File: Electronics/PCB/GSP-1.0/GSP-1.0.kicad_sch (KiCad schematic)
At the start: 14 parts

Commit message: Fix ESP32 version
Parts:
- removed U3: (no value), symbol RF_Module:ESP32-WROOM-32
- added BT1: (no value), symbol Device:Battery_Cell
- added BZ1: (no value), symbol Device:Buzzer
- added C1: (no value), symbol Device:C
- added D_3V3: (no value), symbol Device:LED
- added EN_Pull-up1, R2: 10K, symbol Device:R
- added J_EN1, J_IO_1: Conn_01x01_Male, symbol Connector:Conn_01x01_Male
- added J_UART1: (no value), symbol Connector:Conn_01x06_Male
- added Q1: (no value), symbol Transistor_BJT:BC817
- added Q2: ASS8050-L-HF, Package_TO_SOT_SMD:SOT-23, symbol Transistor_BJT:BC817
- added R1, R_LED1: (no value), symbol Device:R
- added RV_buzzer1: (no value), symbol Device:R_Potentiometer
- added SW_PWR1: (no value), symbol Switch:SW_SPST
- added U1: (no value), symbol GlobalSymbolLibrary:ESP32-S2-WROOM-I
- RV1, RV2: value (none) -> R_Potentiometer
- SW1, SW10, SW2, SW3, SW4, SW5, SW6, SW7, SW8, SW9: value (none) -> SW_Push; footprint (none) -> Button_Switch_SMD:SW_Push_1P1T_NO_CK_KSC6xxJ
- U2: value (none) -> 128x64_2.42"_OLED; footprint (none) -> GlobalLibrary:128x64 2.42 inch OLED display
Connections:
- net +3V3: now also BT1.1 (+), EN_Pull-up1.1, J_UART1.2 (Pin_2), R_LED1.1, U1.2 (3V3)
- net GNDREF: now also SW1.2, SW2.2, SW3.2, SW4.2, SW5.2, SW6.2, SW7.2, SW8.2, BZ1.2 (+), C1.1, D_3V3.1 (K), J_UART1.1 (Pin_1), SW_PWR1.1 (A), U1.1 (GND), U1.26 (GND), U1.42 (GND), U1.43 (GND), U1.44 (GND), U1.45 (GND), U1.46 (GND), U1.47 (GND), U1.48 (GND), U1.49 (GND), U1.50 (GND), U1.51 (GND)
- net IO8: now reaches U2.DC
- net IO8: now also U1.11 (IO8)
- net at U2.RES: now also U1.24 (IO21)
- net at U2.SCL: now also U1.30 (IO36)
- net at U2.SDA: now also U1.29 (IO35)
- new net: Q1.1 (B), R1.2
- new net: Q2.1 (B), R2.2
- new net: BT1.2 (-), SW_PWR1.2 (B)
- new net: BZ1.1 (-), RV_buzzer1.3
- new net: D_3V3.2 (A), R_LED1.2
- new net BUZZER_PIN: RV_buzzer1.1, RV_buzzer1.2, U1.19 (IO16)
- new net DTR: J_UART1.5 (Pin_5), Q2.2 (E), R1.1
- new net EN: C1.2, EN_Pull-up1.2, J_EN1.1 (Pin_1), Q1.3 (C), U1.41 (EN)
- new net IO_0: J_IO_1.1 (Pin_1), Q2.3 (C), U1.3 (IO0)
- new net RTS: J_UART1.6 (Pin_6), Q1.2 (E), R2.1
- new net RX: J_UART1.4 (Pin_4), U1.38 (RXD0)
- new net TX: J_UART1.3 (Pin_3), U1.37 (TXD0)
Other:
- moved on the sheet: RV1, RV2, SW1, SW10, SW2, SW3, SW4, SW5, SW6, SW7, SW8, SW9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

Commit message: Update
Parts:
- removed RV1, RV2: R_Potentiometer, symbol Device:R_Potentiometer
- BT1: value (none) -> Battery_Cell
- BZ1: value (none) -> Buzzer1; footprint (none) -> Buzzer_Beeper:Buzzer_12x9.5RM7.6
- C1: value (none) -> 10uF
- D_3V3: value (none) -> LED
- J_UART1: value (none) -> Conn_01x06_Male
- Q1: value (none) -> ASS8050-L-HF; footprint (none) -> Package_TO_SOT_SMD:SOT-23
- R1: value (none) -> 10K
- R_LED1: value (none) -> R_LED
- SW_PWR1: value (none) -> SW_SPST; footprint (none) -> GustavsGlobalLibrary:Slide-SW-GF-1123-1110
- U1: value (none) -> ESP32-S2-WROOM-I; footprint (none) -> XCVR_ESP32-S2-WROOM-I
- Volume: renamed from RV_buzzer1; value (none) -> R_Buzzer1; footprint (none) -> Potentiometer_THT:Potentiometer_Alps_RK09K_Single_Horizontal
- renumbered SW9 to SELECT, SW10 to START
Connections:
- net GNDREF: now also SELECT.2, START.2
- net IO8: now also SW8.1; no longer U2.DC
- net IO4: now reaches SW4.1
- net IO4: now also U1.7 (IO4)
- net IO3: now reaches SW3.1
- net IO3: now also U1.6 (IO3)
- net IO7: now reaches U1.10 (IO7)
- net IO7: now also SW7.1
- net IO15: now reaches U1.18 (IO15)
- net IO15: now also U2.DC
- net SELECT: now reaches U1.35 (IO41)
- net SELECT: now also SELECT.1
- net START: now reaches U1.36 (IO42)
- net START: now also START.1
- net IO1: now reaches U1.4 (IO1)
- net IO1: now also SW1.1
- net IO2: now reaches U1.5 (IO2)
- net IO2: now also SW2.1
- net IO5: now reaches U1.8 (IO5)
- net IO5: now also SW5.1
- net IO6: now reaches U1.9 (IO6)
- net IO6: now also SW6.1
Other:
- moved on the sheet: BZ1, R_LED1, SELECT, START, Volume

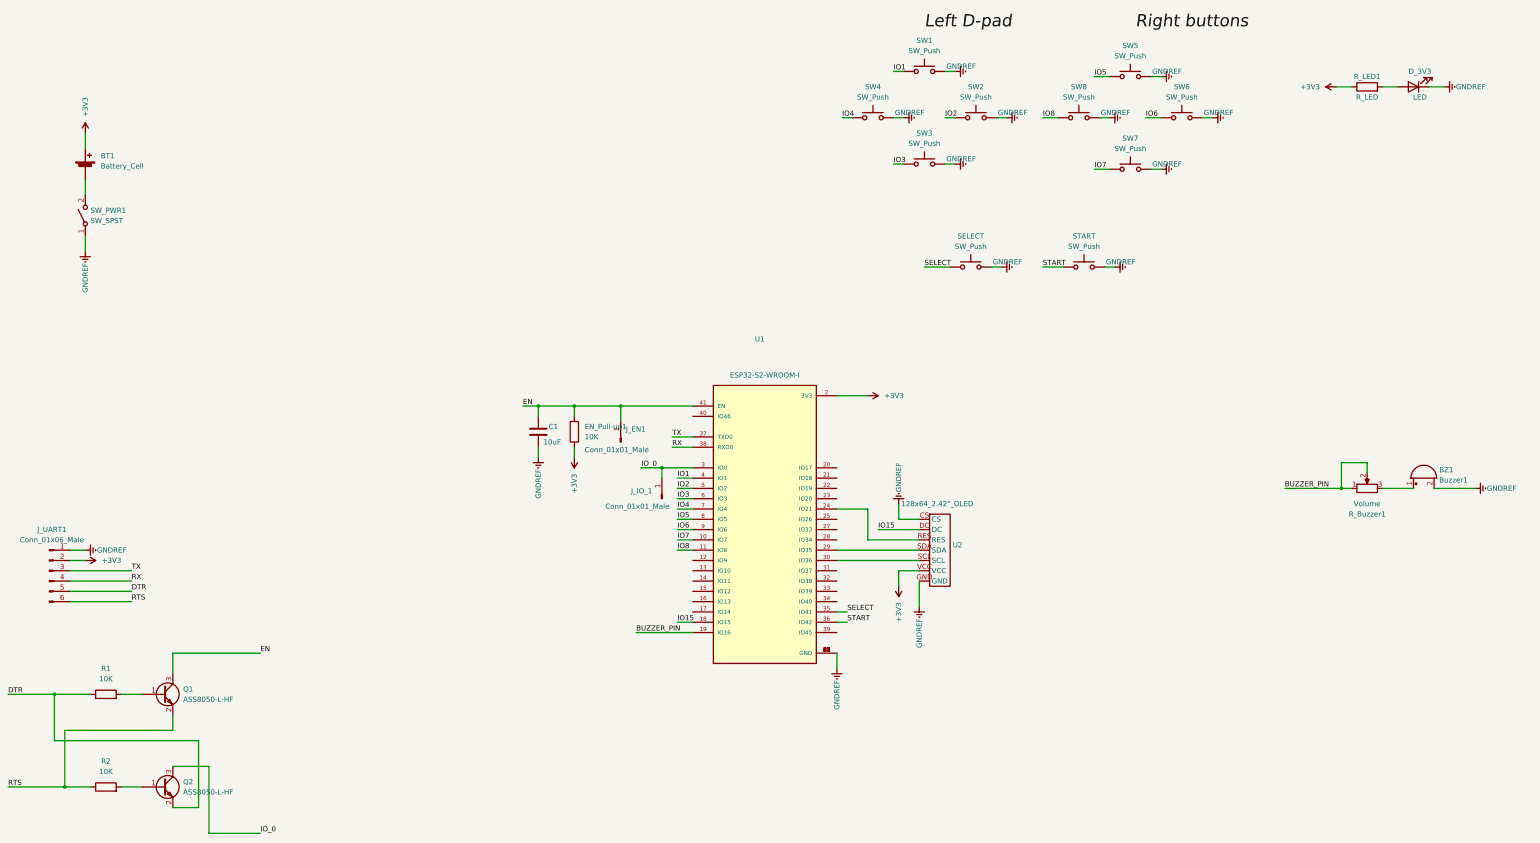
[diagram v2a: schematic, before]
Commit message: PCB almost finished, but lots of errors
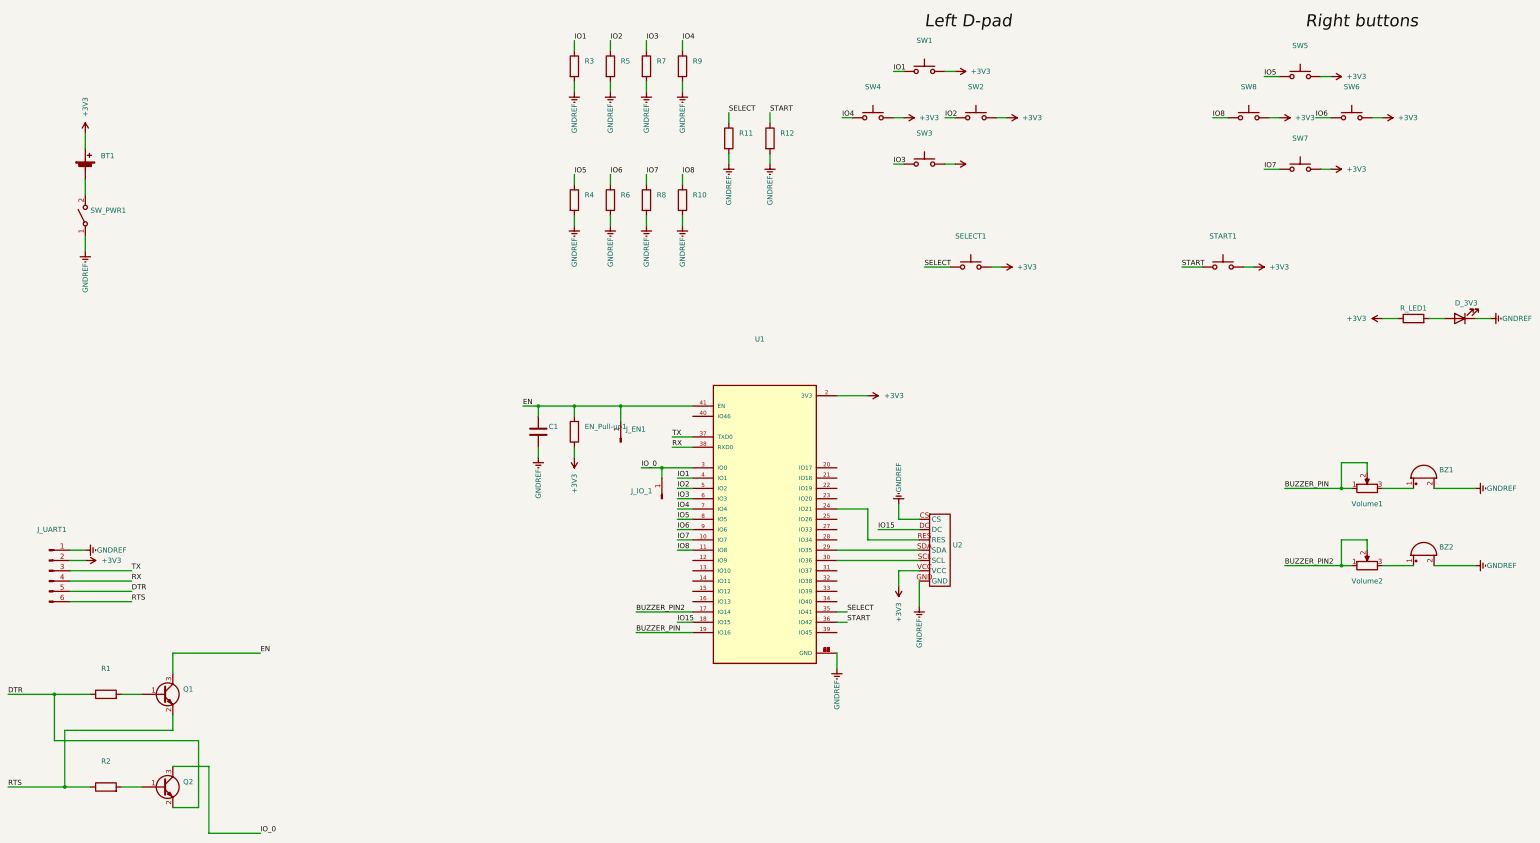
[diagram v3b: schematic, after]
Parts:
- added BZ2: (no value), symbol Device:Buzzer
- added R10, R11, R12, R3, R4, R5, R6, R7, R8, R9: (no value), symbol Device:R
- added Volume2: (no value), symbol Device:R_Potentiometer
- BT1: value Battery_Cell -> (none)
- BZ1: value Buzzer1 -> (none); footprint Buzzer_Beeper:Buzzer_12x9.5RM7.6 -> (none)
- C1: value 10uF -> (none)
- D_3V3: value LED -> (none)
- EN_Pull-up1, R1, R2: value 10K -> (none)
- J_EN1, J_IO_1: value Conn_01x01_Male -> (none)
- J_UART1: value Conn_01x06_Male -> (none)
- Q1, Q2: value ASS8050-L-HF -> (none); footprint Package_TO_SOT_SMD:SOT-23 -> (none)
- R_LED1: value R_LED -> (none)
- SELECT1: renamed from SELECT; value SW_Push -> (none); footprint Button_Switch_SMD:SW_Push_1P1T_NO_CK_KSC6xxJ -> (none)
- START1: renamed from START; value SW_Push -> (none); footprint Button_Switch_SMD:SW_Push_1P1T_NO_CK_KSC6xxJ -> (none)
- SW1, SW2, SW3, SW4, SW5, SW6, SW7, SW8: value SW_Push -> (none); footprint Button_Switch_SMD:SW_Push_1P1T_NO_CK_KSC6xxJ -> (none)
- SW_PWR1: value SW_SPST -> (none); footprint GustavsGlobalLibrary:Slide-SW-GF-1123-1110 -> (none)
- U1: value ESP32-S2-WROOM-I -> (none); footprint XCVR_ESP32-S2-WROOM-I -> (none)
- U2: value 128x64_2.42"_OLED -> (none); footprint GlobalLibrary:128x64 2.42 inch OLED display -> (none)
- Volume1: renamed from Volume; value R_Buzzer1 -> (none); footprint Potentiometer_THT:Potentiometer_Alps_RK09K_Single_Horizontal -> (none)
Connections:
- net +3V3: now also SELECT1.2, START1.2, SW1.2, SW2.2, SW3.2, SW4.2, SW5.2, SW6.2, SW7.2, SW8.2
- net GNDREF: now also BZ2.2 (+), R10.2, R11.2, R12.2, R3.2, R4.2, R5.2, R6.2, R7.2, R8.2, R9.2; no longer SELECT1.2, START1.2, SW1.2, SW2.2, SW3.2, SW4.2, SW5.2, SW6.2, SW7.2, SW8.2
- net IO1: now also R3.1
- net IO2: now also R5.1
- net IO3: now also R7.1
- net IO4: now also R9.1
- net IO5: now also R4.1
- net IO6: now also R6.1
- net IO7: now also R8.1
- net IO8: now also R10.1
- net SELECT: now also R11.1
- net START: now also R12.1
- net BUZZER_PIN2: now reaches U1.17 (IO14)
- net BUZZER_PIN2: now also Volume2.1, Volume2.2
- new net: BZ2.1 (-), Volume2.3
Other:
- moved on the sheet: D_3V3, R_LED1, START1, SW5, SW6, SW7, SW8

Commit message: Fix PCB
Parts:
- added C2: 22uF, symbol Device:C
- added C3: 0.1uF, symbol Device:C
- added J1: (no value), symbol Connector:USB_C_Receptacle_USB2.0
- added R13, R14: 5.1K, Resistor_SMD:R_0805_2012Metric_Pad1.20x1.40mm_HandSolder, symbol Device:R_Small
- added U3: (no value), symbol Regulator_Linear:AZ1117-3.3
- added U4: AZ1117-3.3, Package_TO_SOT_SMD:SOT-223-3_TabPin2, symbol Regulator_Linear:AZ1117-3.3
- BT1: value (none) -> Battery_pack; footprint (none) -> GustavsGlobalLibrary:3xAA holder (534-2464)
- BZ1: value (none) -> Buzzer1; footprint (none) -> Buzzer_Beeper:Buzzer_12x9.5RM7.6
- BZ2: value (none) -> Buzzer2; footprint (none) -> Buzzer_Beeper:Buzzer_12x9.5RM7.6
- C1: value (none) -> 10uF; footprint (none) -> Capacitor_SMD:C_0805_2012Metric_Pad1.18x1.45mm_HandSolder
- D_3V3: footprint (none) -> LED_SMD:LED_0805_2012Metric_Pad1.15x1.40mm_HandSolder
- EN_Pull-up1, R1, R10, R11, R12, R2, R3, R4, R5, R6, R7, R8, R9: value (none) -> 10K; footprint (none) -> Resistor_SMD:R_0805_2012Metric_Pad1.20x1.40mm_HandSolder
- J_EN1, J_IO_1: value (none) -> Conn_01x01_Male
- J_UART1: value (none) -> Conn_01x06_Male
- Q1, Q2: value (none) -> ASS8050-L-HF; footprint (none) -> Package_TO_SOT_SMD:SOT-23
- R_LED1: value (none) -> R_LED; footprint (none) -> Resistor_SMD:R_0805_2012Metric_Pad1.20x1.40mm_HandSolder
- SELECT1, START1: footprint (none) -> Button_Switch_SMD:SW_Push_1P1T_NO_CK_KSC6xxJ
- SW1, SW2, SW3, SW4, SW5, SW6, SW7, SW8: value (none) -> SW_Push; footprint (none) -> Button_Switch_SMD:SW_Push_1P1T_NO_CK_KSC6xxJ
- SW_PWR1: value (none) -> SW_SPST; footprint (none) -> GustavsGlobalLibrary:Slide-SW-GF-1123-1110
- U1: value (none) -> ESP32-S2-WROOM-I
- U2: value (none) -> 128x64_2.42"_OLED; footprint (none) -> GlobalLibrary:128x64 2.42 inch OLED display
- Volume1: value (none) -> R_Buzzer1; footprint (none) -> Potentiometer_THT:Potentiometer_Alps_RK09K_Single_Horizontal
- Volume2: value (none) -> R_Buzzer2; footprint (none) -> Potentiometer_THT:Potentiometer_Alps_RK09K_Single_Horizontal
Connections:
- net +3V3: now also C2.1, C3.1, U3.2 (VO), U4.2 (VO); no longer BT1.1 (+)
- net GNDREF: now also C2.2, C3.2, J1.A1 (GND), J1.A12 (GND), J1.B1 (GND), J1.B12 (GND), J1.S1 (SHIELD), R13.2, R14.2, U3.1 (GND), U4.1 (GND)
- net D-: now reaches U1.22 (IO19)
- net D-: now also J1.A7 (D-), J1.B7 (D-)
- net D+: now reaches U1.23 (IO20)
- net D+: now also J1.A6 (D+), J1.B6 (D+)
- new net: J1.A5 (CC1), R13.1
- new net: BT1.1 (+), U3.3 (VI)
- new net: J1.B5 (CC2), R14.1
- new net +5V: J1.A4 (VBUS), J1.A9 (VBUS), J1.B4 (VBUS), J1.B9 (VBUS), U4.3 (VI)

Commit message: Update PCB
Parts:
- C2, C3: footprint (none) -> Capacitor_SMD:C_0805_2012Metric_Pad1.18x1.45mm_HandSolder
- D_3V3: value (none) -> PWR
- J1: value (none) -> USB_C_Receptacle_USB2.0; footprint (none) -> Connector_USB:USB_C_Receptacle_HRO_TYPE-C-31-M-12
- J_EN1, J_IO_1: footprint (none) -> Connector_PinHeader_1.27mm:PinHeader_1x01_P1.27mm_Vertical
- J_UART1: footprint (none) -> Connector_PinHeader_1.27mm:PinHeader_1x06_P1.27mm_Vertical
- SELECT1: value (none) -> SELECT
- START1: value (none) -> START
- U1: footprint (none) -> GustavsGlobalLibrary:XCVR_ESP32-S2-WROOM-I
- U3: value (none) -> AZ1117-3.3; footprint (none) -> Package_TO_SOT_SMD:SOT-223-3_TabPin2
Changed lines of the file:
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@@
     (property "Reference" "U1" (id 0) (at 208.28 104.14 0))
     (property "Value" "ESP32-S2-WROOM-I" (id 1) (at 209.55 113.03 0))
-    (property "Footprint" "" (id 2) (at 209.55 151.13 0)
+    (property "Footprint" "GustavsGlobalLibrary:XCVR_ESP32-S2-WROOM-I" (id 2) (at 209.55 151.13 0)
       (effects (font (size 1.27 1.27)) (justify left bottom) hide)
     )
@@
     (property "Reference" "J_UART1" (id 0) (at 33.655 151.13 0))
     (property "Value" "Conn_01x06_Male" (id 1) (at 33.655 153.67 0))
-    (property "Footprint" "" (id 2) (at 33.02 161.29 0)
+    (property "Footprint" "Connector_PinHeader_1.27mm:PinHeader_1x06_P1.27mm_Vertical" (id 2) (at 33.02 161.29 0)
       (effects (font (size 1.27 1.27)) hide)
     )
@@
       (effects (font (size 1.27 1.27)) (justify left))
     )
-    (property "Footprint" "" (id 2) (at 98.7552 50.8 0)
+    (property "Footprint" "Capacitor_SMD:C_0805_2012Metric_Pad1.18x1.45mm_HandSolder" (id 2) (at 98.7552 50.8 0)
       (effects (font (size 1.27 1.27)) hide)
     )
@@
     (in_bom yes) (on_board yes)
     (property "Reference" "SELECT1" (id 0) (at 260.35 78.74 0))
-    (property "Value" "" (id 1) (at 260.35 81.28 0))
+    (property "Value" "SELECT" (id 1) (at 260.35 81.28 0))
     (property "Footprint" "Button_Switch_SMD:SW_Push_1P1T_NO_CK_KSC6xxJ" (id 2) (at 260.35 81.28 0)
       (effects (font (size 1.27 1.27)) hide)
@@
       (effects (font (size 1.27 1.27)) (justify left))
     )
-    (property "Footprint" "" (id 2) (at 111.4552 50.8 0)
+    (property "Footprint" "Capacitor_SMD:C_0805_2012Metric_Pad1.18x1.45mm_HandSolder" (id 2) (at 111.4552 50.8 0)
       (effects (font (size 1.27 1.27)) hide)
     )
@@
       (effects (font (size 1.27 1.27)) (justify right))
     )
-    (property "Footprint" "" (id 2) (at 173.99 129.54 0)
+    (property "Footprint" "Connector_PinHeader_1.27mm:PinHeader_1x01_P1.27mm_Vertical" (id 2) (at 173.99 129.54 0)
       (effects (font (size 1.27 1.27)) hide)
     )
@@
       (effects (font (size 1.27 1.27)) hide)
     )
-    (property "Value" "" (id 1) (at 64.77 107.9499 90)
+    (property "Value" "+5V" (id 1) (at 64.77 107.9499 90)
       (effects (font (size 1.27 1.27)) (justify left))
     )
@@
     (in_bom yes) (on_board yes) (fields_autoplaced)
     (property "Reference" "J1" (id 0) (at 41.91 100.33 0))
-    (property "Value" "" (id 1) (at 41.91 102.87 0))
-    (property "Footprint" "" (id 2) (at 45.72 123.19 0)
+    (property "Value" "USB_C_Receptacle_USB2.0" (id 1) (at 41.91 102.87 0))
+    (property "Footprint" "Connector_USB:USB_C_Receptacle_HRO_TYPE-C-31-M-12" (id 2) (at 45.72 123.19 0)
       (effects (font (size 1.27 1.27)) hide)
     )
@@
     (in_bom yes) (on_board yes)
     (property "Reference" "START1" (id 0) (at 322.58 78.74 0))
-    (property "Value" "" (id 1) (at 322.58 81.28 0))
+    (property "Value" "START" (id 1) (at 322.58 81.28 0))
     (property "Footprint" "Button_Switch_SMD:SW_Push_1P1T_NO_CK_KSC6xxJ" (id 2) (at 322.58 81.28 0)
       (effects (font (size 1.27 1.27)) hide)
@@
     (in_bom yes) (on_board yes)
     (property "Reference" "D_3V3" (id 0) (at 382.5875 95.25 0))
-    (property "Value" "" (id 1) (at 382.5875 101.6 0))
+    (property "Value" "PWR" (id 1) (at 382.5875 101.6 0))
     (property "Footprint" "LED_SMD:LED_0805_2012Metric_Pad1.15x1.40mm_HandSolder" (id 2) (at 381 99.06 0)
       (effects (font (size 1.27 1.27)) hide)
@@
       (effects (font (size 1.27 1.27)) (justify left))
     )
-    (property "Value" "" (id 1) (at 38.1 48.2599 90)
-      (effects (font (size 1.27 1.27)) (justify left))
-    )
-    (property "Footprint" "" (id 2) (at 35.56 46.99 0)
+    (property "Value" "AZ1117-3.3" (id 1) (at 38.1 48.2599 90)
+      (effects (font (size 1.27 1.27)) (justify left))
+    )
+    (property "Footprint" "Package_TO_SOT_SMD:SOT-223-3_TabPin2" (id 2) (at 35.56 46.99 0)
       (effects (font (size 1.27 1.27) italic) hide)
     )
@@
       (effects (font (size 1.27 1.27)) (justify right))
     )
-    (property "Footprint" "" (id 2) (at 184.15 143.51 0)
-      (effects (font (size 1.27 1.27)) hide)
-    )
+    (property "Footprint" "Connector_PinHeader_1.27mm:PinHeader_1x01_P1.27mm_Vertical" (id 2) (at 184.15 143.51 0)
+      (effects (font (size 1.27 1.27)) hide)
+    )
